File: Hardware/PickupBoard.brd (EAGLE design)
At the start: 49.9 x 29 mm, 29 parts, among them T1 2N3904, U1 TL074_

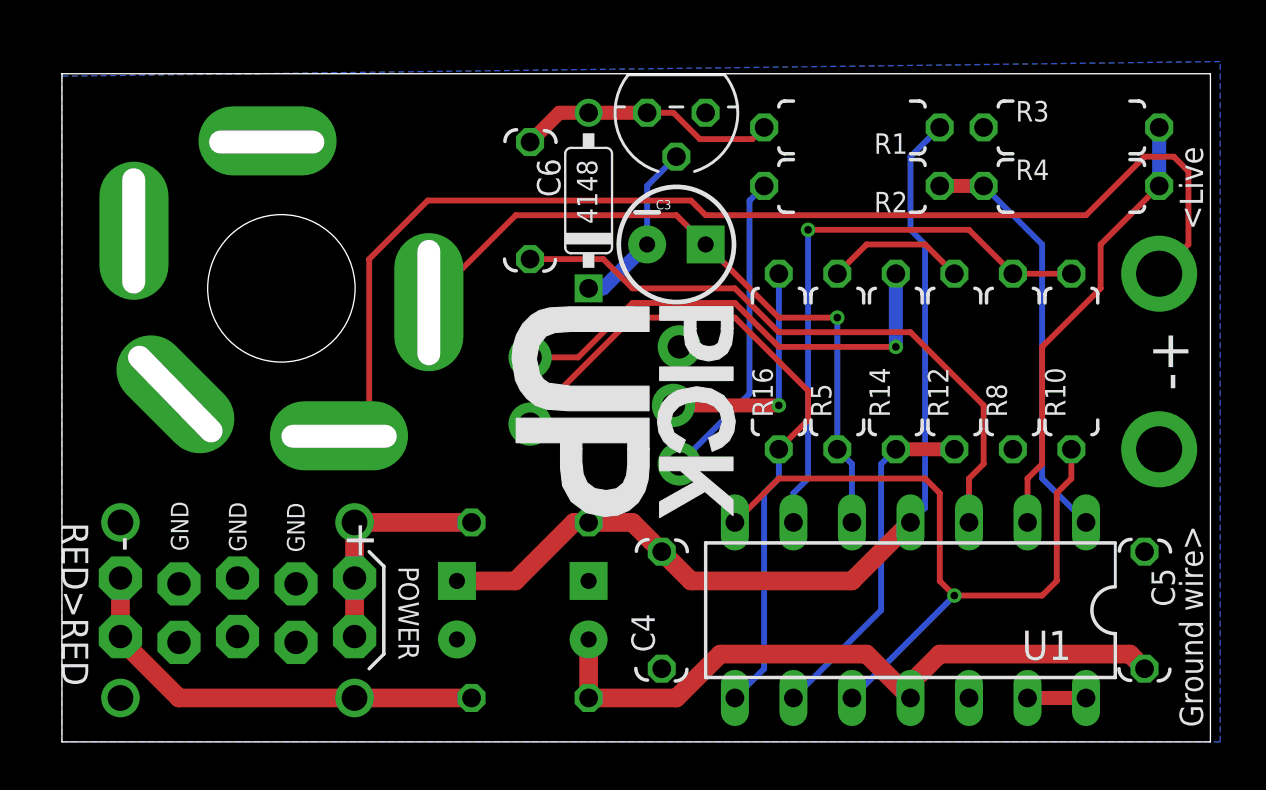
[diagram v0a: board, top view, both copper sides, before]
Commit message: Rev2 Pickup Board finished and routed
Panel and Daughterboard unchanged fixes #2, fixes #3, fixes #4
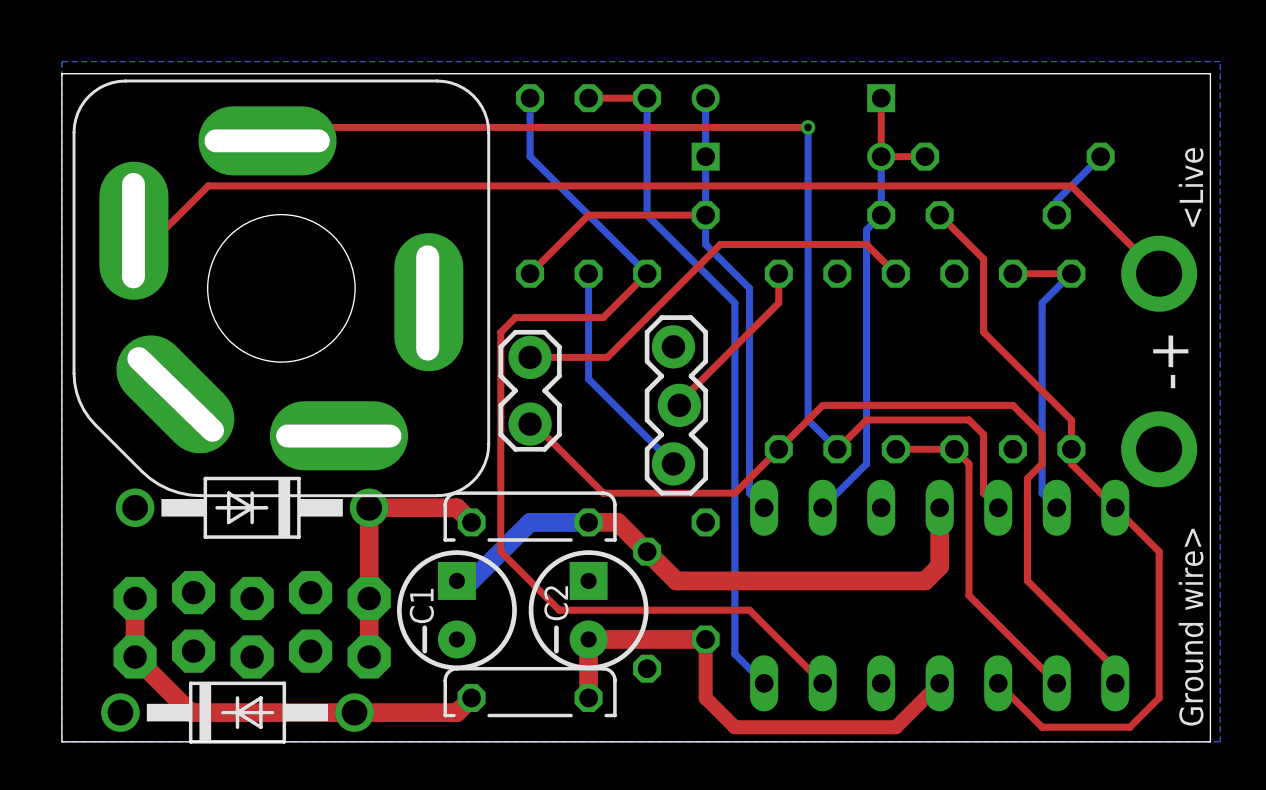
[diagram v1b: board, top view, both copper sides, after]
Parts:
- removed 4148: (no value), MusicThingModular:DO35-7
- removed C6: 100n, TomW:C050-024X044
- removed T1: 2N3904, transistor:TO92
- added D1, D2: 1N4148, MusicThingModular:DO35-7
- added R6: 10k, MusicThingModular:7MM_RESISTOR
- C3: value 4.7uf -> 100n; device SparkFun-Passives:CPOL-RADIAL-10UF-25V -> TomW:C050-024X044
- R1: value 100k -> 1k
- R3: value 2.2k -> 100k
- R4: value 22k -> 1.2K
- moved R4 23.5 mm to (20.3, 24.1), flipped to the bottom, turned to 270 degrees
- moved C5 19.1 mm to (27.9, 6.99), flipped to the bottom
- moved C3 14.0 mm to (40.6, 22.9), flipped to the bottom
- moved R3 12.7 mm to (31.8, 22.9), flipped to the bottom, turned to 180 degrees
- moved R2 11.4 mm to (22.9, 24.1), flipped to the bottom, turned to 270 degrees
- moved R1 7.10 mm to (41.3, 25.4), flipped to the bottom, turned to 0 degrees
- moved U1 1.42 mm to (38.1, 6.35), flipped to the bottom
- moved D5 0.90 mm to (8.26, 10.2), flipped to the top, turned to 180 degrees
- moved U$2 0.90 mm to (8.26, 5.08), flipped to the bottom, turned to 180 degrees
- moved C4 0.64 mm to (25.4, 5.71), flipped to the bottom
- moved D6 0.64 mm to (7.62, 1.27), flipped to the top, turned to 0 degrees
- flipped 1 to the top, turned to 0 degrees
- flipped C1 to the top
- flipped C2 to the top
- flipped FUSE to the top, turned to 0 degrees
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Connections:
- removed net N$12: R2.1, R4.1, U1.1
- net +12V: no longer R1.1
- net FUZZ_IN: now also C3.2, R10.1, U1.10, U1.7; no longer C3.1, R5.1, U$1.TIP, U1.5
- net GND: now also U1.3; no longer R3.1, T1.3
- net N$1: now also R5.1, U$1.TIP, U1.5; no longer C6.2, U1.3
- net N$11: now also R2.1, R6.1, U1.14; no longer R3.2, R4.2, U1.2
- net N$2: now also D1.C, D2.A, R3.1, R4.2, U1.1; no longer U1.13, U1.14
- net N$4: now also D1.A, D2.C, R1.2, R3.2, U1.2; no longer R10.1, U1.10, U1.7
- net N$7: now also C3.1, R1.1; no longer 4148.C, C3.2, T1.2
- net N$9: now also R4.1, R6.2, U1.13; no longer 4148.A, C6.1, R1.2, T1.1
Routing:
- net N$9: track 11.4 -> 43.0 mm
- net N$2: track 2.54 -> 27.5 mm
- net N$1: track 27.7 -> 48.8 mm, vias 0 -> 1
- net N$12: track 18.4 -> 0.00 mm
- net +12V: track 41.0 -> 25.9 mm
- net N$3: track 25.2 -> 13.5 mm, vias 1 -> 0
- net N$4: track 31.6 -> 20.7 mm, vias 1 -> 0
- net N$11: track 19.5 -> 30.0 mm
- net N$8: track 30.0 -> 38.2 mm
- net -12V: track 29.7 -> 21.6 mm
- net GND: track 6.13 -> 0.00 mm
- net N$14: track 51.4 -> 46.9 mm
- net N$7: track 7.67 -> 3.33 mm
- net N$13: track 13.6 -> 9.78 mm
- net FUZZ_IN: track 30.3 -> 33.2 mm, vias 1 -> 0
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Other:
- board text added: "Revision 2 PCB"
- board text removed: "1"
- board text removed: "NB: Only marked parts on this side -> Rest on the other side"
- board text removed: "Revision 1 PCB"

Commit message: Value changes + new cap
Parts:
- removed R3: 100k, MusicThingModular:7MM_RESISTOR
- added C6: 470pf, TomW:C050-024X044
- C3: value 100n -> 470n
- R1: value 1k -> 10k
- R4: value 1.2K -> 10k
- R6: value 10k -> 100k
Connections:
- net N$2: now also C6.1; no longer R3.1
- net N$4: now also C6.2; no longer R3.2
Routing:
- net N$2: track 27.5 -> 28.7 mm
- net N$4: track 20.7 -> 21.3 mm

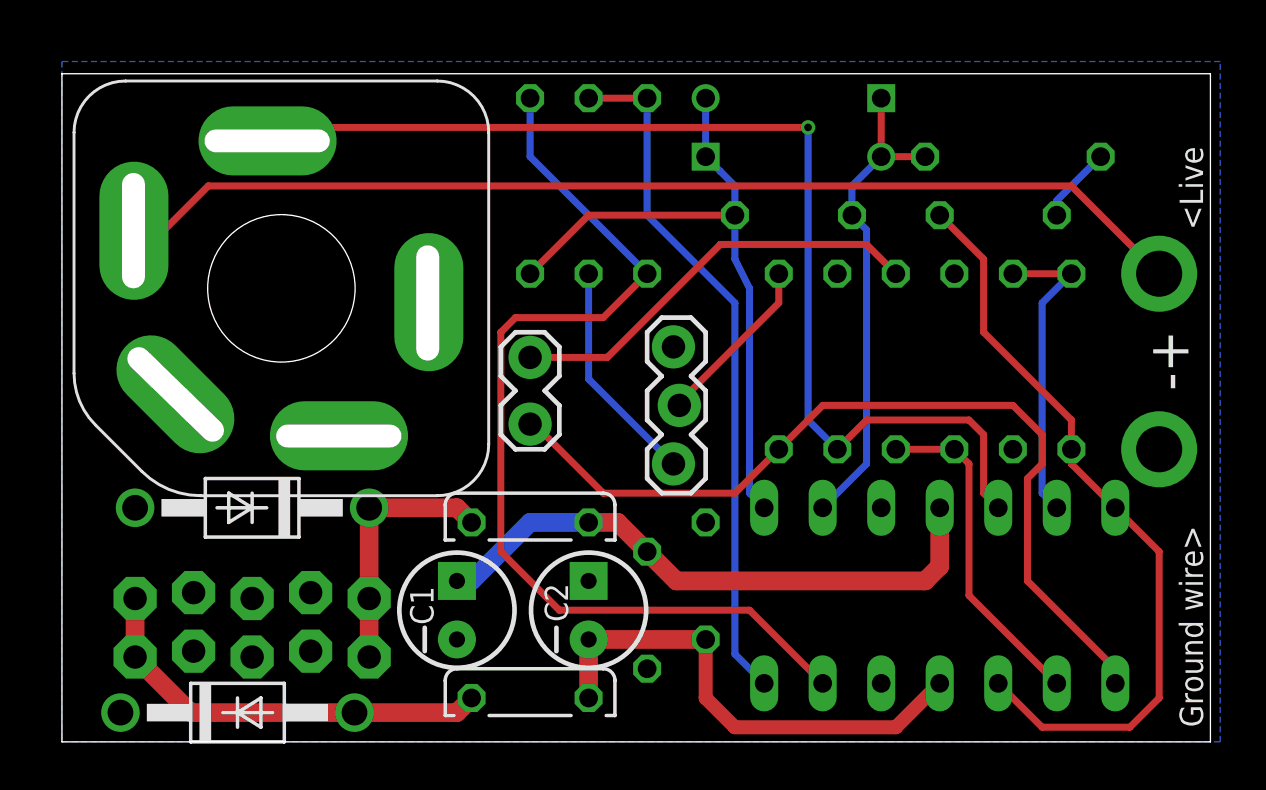
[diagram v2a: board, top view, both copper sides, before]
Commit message: Small routing changes
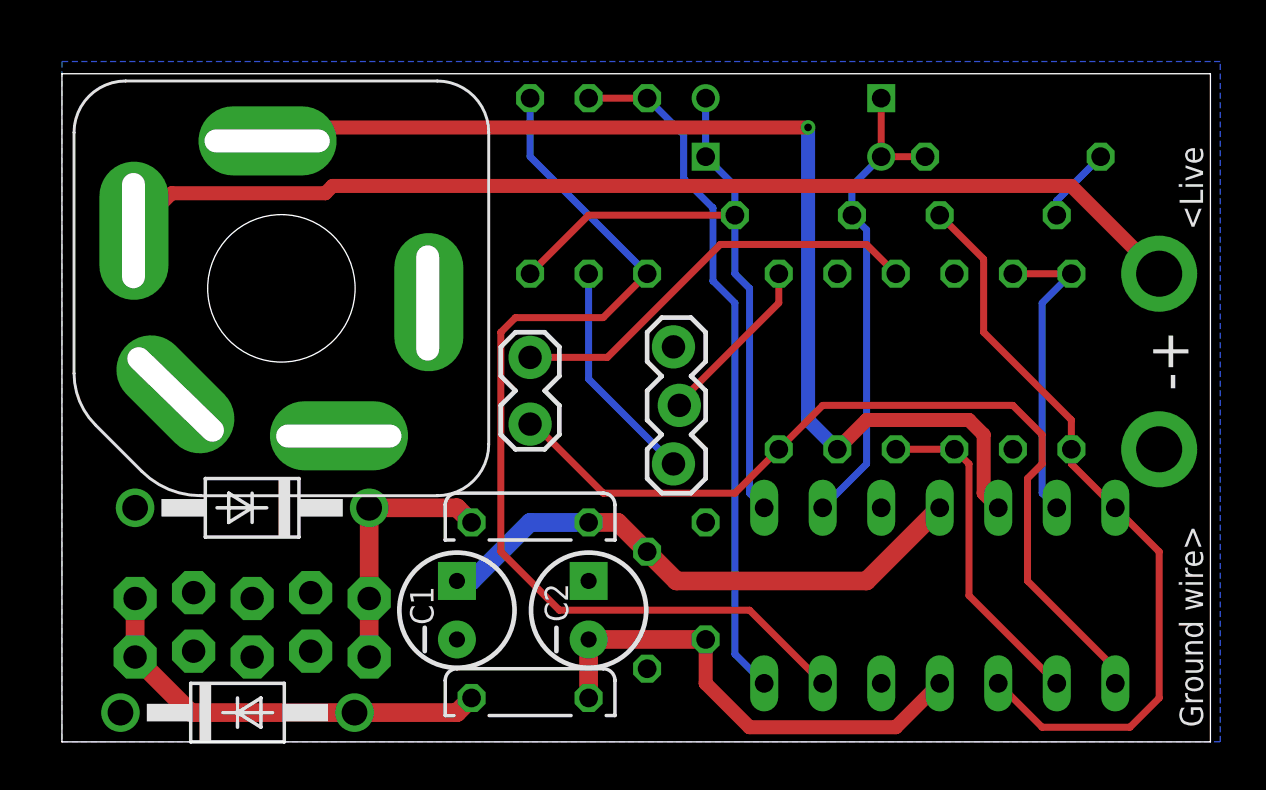
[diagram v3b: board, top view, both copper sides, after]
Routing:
- net +12V: track 25.9 -> 24.4 mm
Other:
- board text added: "Revision 3 PCB"
- board text removed: "Revision 2 PCB"

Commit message: Reworked layout to reduce noise / feedback
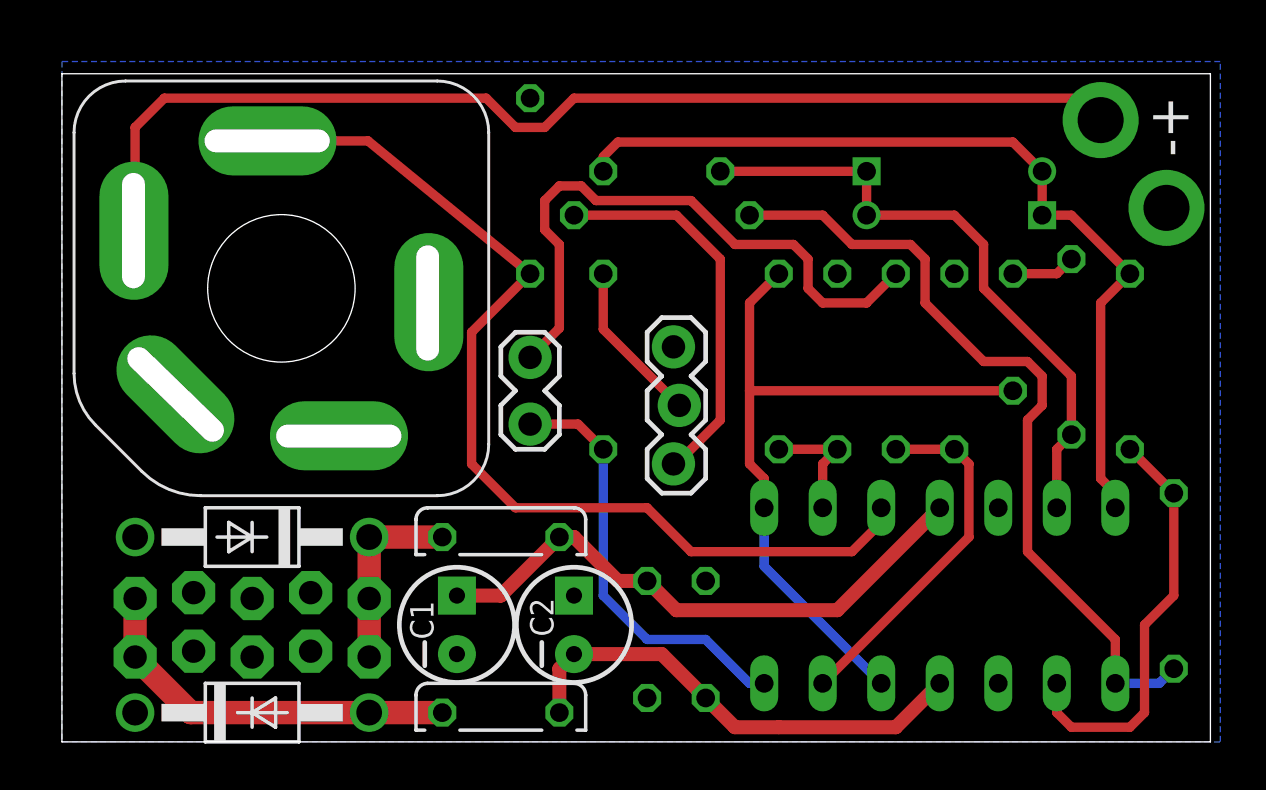
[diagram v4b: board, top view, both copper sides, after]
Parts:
- moved R6 28.6 mm to (48.3, 6.99)
- moved R4 27.1 mm to (46.4, 16.5), turned to 90 degrees
- moved R5 15.4 mm to (20.3, 24.1)
- moved R10 12.7 mm to (31.1, 16.5), turned to 270 degrees
- moved JP4 10.5 mm to (47.9, 23.2)
- moved R1 8.64 mm to (43.8, 17.1), turned to 270 degrees
- moved D2 7.67 mm to (38.7, 24.8), turned to 180 degrees
- moved R16 7.62 mm to (23.5, 16.5)
- moved R8 7.62 mm to (33.7, 16.5), turned to 270 degrees
- moved D1 7.43 mm to (38.7, 22.9), turned to 0 degrees
- moved JP3 7.13 mm to (45.1, 27.0)
- moved C6 6.02 mm to (26.0, 24.8)
- moved C3 5.12 mm to (41.3, 17.8), turned to 270 degrees
- moved R2 3.42 mm to (26.0, 22.9), turned to 0 degrees
- moved C5 2.54 mm to (27.9, 4.45)
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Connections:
- net FUZZ_IN: now also U1.1, U1.12; no longer U1.10, U1.7
- net GND: now also R12.1, U1.10, U1.5; no longer R12.2, U1.12, U1.3
- net N$1: now also U1.3; no longer U1.5
- net N$11: now also R6.2, U1.8; no longer R6.1, U1.14
- net N$2: now also U1.7; no longer U1.1
- net N$3: now also U1.2; no longer U1.6
- net N$4: now also U1.6; no longer U1.2
- net N$5: now also R14.1; no longer R14.2
- net N$6: now also R12.2, R14.2, U1.13; no longer R12.1, R14.1, U1.9
- net N$8: now also U1.14; no longer U1.8
- net N$9: now also R6.1, U1.9; no longer R6.2, U1.13
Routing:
- net N$9: track 43.0 -> 18.4 mm
- net N$8: track 38.2 -> 18.5 mm
- net N$2: track 28.8 -> 38.2 mm
- net N$3: track 13.5 -> 5.34 mm
- net N$5: track 18.4 -> 26.5 mm
- net N$13: track 9.78 -> 16.9 mm
- net N$4: track 21.3 -> 27.1 mm
- net N$1: track 48.8 -> 43.3 mm, vias 1 -> 0
- net N$11: track 30.0 -> 34.7 mm
- net +12V_INLET: track 11.2 -> 8.38 mm
- net -12V_INLET: track 18.4 -> 16.9 mm
- net N$14: track 46.9 -> 48.4 mm
- net FUZZ_IN: track 33.2 -> 32.1 mm
- net N$6: track 14.5 -> 15.6 mm
- net +12V: track 24.4 -> 25.2 mm
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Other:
- board text added: "Revision 4 PCB"
- board text removed: "<Live"
- board text removed: "Ground wire>"
- board text removed: "Revision 3 PCB"

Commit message: Rev 4 pcb
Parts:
- moved C6 16.1 mm to (41.3, 19.7), turned to 90 degrees
- moved R2 11.1 mm to (36.2, 18.4), turned to 270 degrees
- moved C3 9.71 mm to (31.8, 15.9), turned to 0 degrees
- moved R8 9.16 mm to (28.6, 24.1)
- moved R10 9.16 mm to (26.0, 24.1)
- moved D1 8.82 mm to (46.4, 18.4), turned to 270 degrees
- moved R14 8.64 mm to (31.1, 23.5)
- moved R12 8.64 mm to (33.7, 23.5)
- moved D2 8.13 mm to (43.8, 18.4), turned to 90 degrees
- moved R1 5.24 mm to (38.7, 18.4), turned to 90 degrees
- moved JP3 5.08 mm to (40.0, 27.0)
- moved JP4 3.86 mm to (47.3, 27.0)
- moved R4 3.18 mm to (48.9, 18.4)
- moved R6 0.64 mm to (48.3, 6.35)
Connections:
- net N$2: now also C6.2; no longer C6.1
- net N$4: now also C6.1; no longer C6.2
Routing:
- net N$6: track 15.6 -> 36.7 mm, vias 0 -> 1
- net N$2: track 38.2 -> 21.0 mm
- net N$4: track 27.1 -> 17.0 mm
- net N$3: track 5.34 -> 14.5 mm
- net N$11: track 34.7 -> 26.2 mm
- net N$5: track 26.5 -> 19.2 mm
- net N$13: track 16.9 -> 11.0 mm
- net N$14: track 48.4 -> 44.0 mm
- net N$7: track 2.80 -> 4.97 mm
- net N$9: track 18.4 -> 19.7 mm
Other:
- board text added: "+-"
- board text removed: "-+"
